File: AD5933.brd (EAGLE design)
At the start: 82.8 x 53.3 mm, 80 parts, among them U1 ADG1604BRUZ, U10 ADP3303ARZ-3.3, U11 AD5242BRZ1M, U12 AD5245BRJZ100-R2, U2 AD5933YRSZ, U3 AD5242BRZ1M, U4 AD8606ARZ, U5 ADG1604BRUZ, U7 AD8606ARZ, U8 LTC6904MPMS8TRPBF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

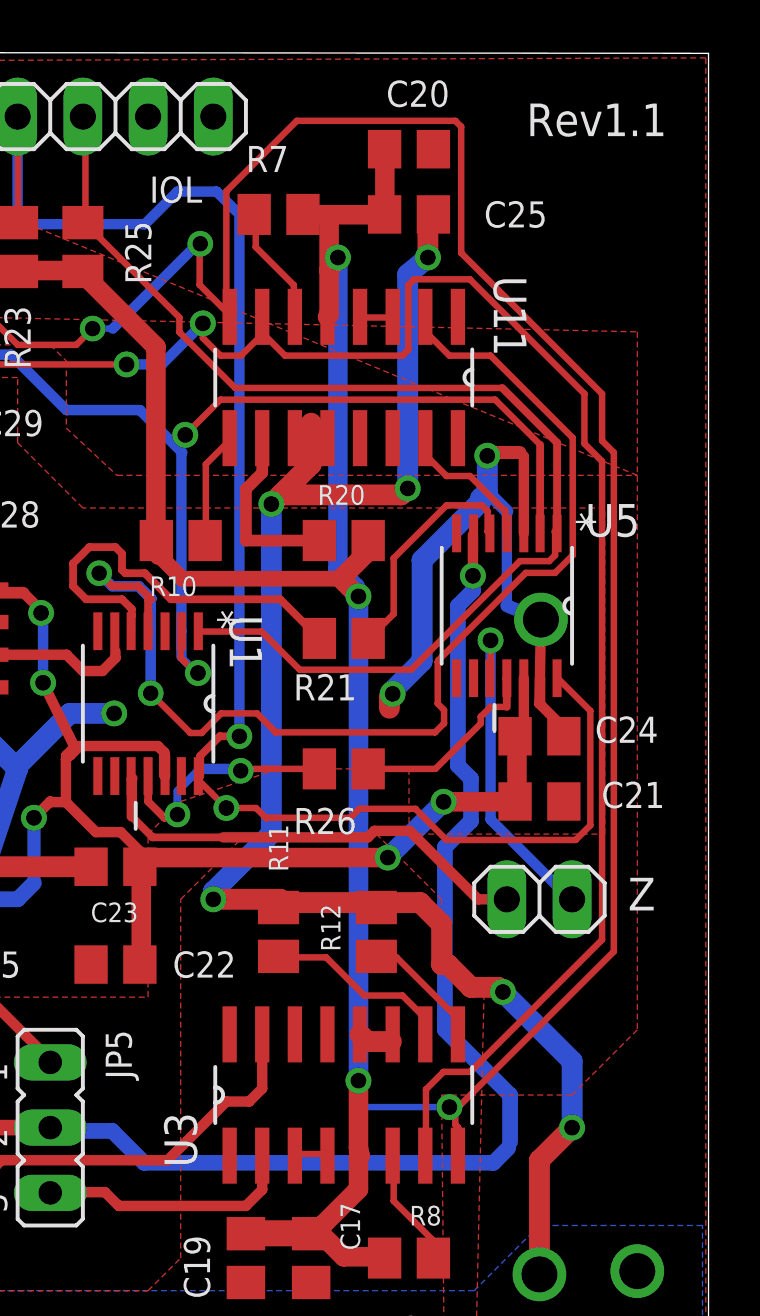
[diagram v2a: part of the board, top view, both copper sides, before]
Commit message: Fixed ad5242 open ckt bug, rev 1.2
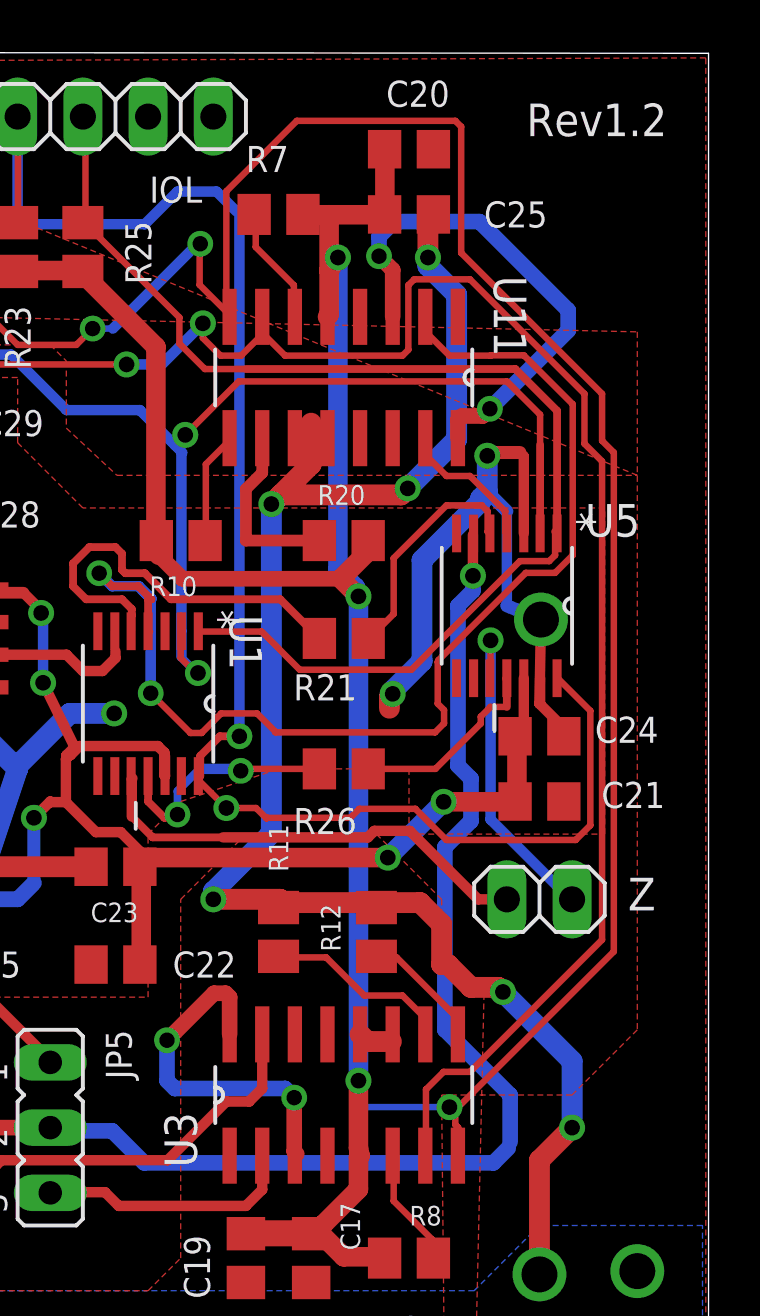
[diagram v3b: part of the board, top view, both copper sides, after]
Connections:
- net U11_W1: now also U11.16; no longer U11.4
- net U3_W1: now also U3.16; no longer U3.4
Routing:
- net U11_W1: track 1.28 -> 19.7 mm, vias 0 -> 2
- net U3_W1: track 1.32 -> 13.8 mm, vias 0 -> 2
- net EN1: track 57.2 -> 58.5 mm
- net A01: track 47.4 -> 48.4 mm
- net GND: track 193.5 -> 194.4 mm
- net U1_S1: track 45.5 -> 46.3 mm
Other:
- board text added: "Rev1.2"
- board text removed: "Rev1.1"
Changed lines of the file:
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@@
 <wire x1="82.784" y1="53.263403125" x2="0.031021875" y2="53.3354375" width="0" layer="20"/>
 <wire x1="0.031021875" y1="53.3354375" x2="0" y2="0" width="0" layer="20"/>
-<text x="75.692" y="50.038" size="1.27" layer="25">Rev1.1</text>
+<text x="75.692" y="50.038" size="1.27" layer="25">Rev1.2</text>
 <text x="66.167" y="3.048" size="1.016" layer="25">IDEA Lab, UTD</text>
 <text x="65.024" y="1.524" size="1.016" layer="25">Athul Asokan Thulasi</text>
@@
 <wire x1="62.2935" y1="30.7467" x2="62.2554" y2="30.7594" width="0.254" layer="1"/>
 <wire x1="53.3781" y1="50.7492" x2="53.34" y2="50.8" width="0.254" layer="16"/>
-<wire x1="63.7794" y1="39.7764" x2="74.4728" y2="39.7764" width="0.254" layer="1"/>
-<wire x1="62.4078" y1="38.4048" x2="63.7794" y2="39.7764" width="0.254" layer="1"/>
+<wire x1="62.4078" y1="38.4048" x2="64.4906" y2="40.4876" width="0.254" layer="1"/>
 <wire x1="62.00775" y1="38.00475" x2="62.4078" y2="38.4048" width="0.4064" layer="16"/>
 <wire x1="53.3781" y1="50.7492" x2="53.3781" y2="46.7487" width="0.254" layer="1"/>
@@
 <wire x1="62.8142" y1="29.1338" x2="62.9031" y2="29.1338" width="0.6096" layer="16"/>
 <wire x1="76.2254" y1="34.5694" x2="76.2254" y2="38.0238" width="0.3048" layer="1"/>
-<wire x1="76.2254" y1="38.0238" x2="74.4728" y2="39.7764" width="0.254" layer="1"/>
 <wire x1="62.9031" y1="29.1338" x2="62.8142" y2="29.1338" width="0.254" layer="1"/>
 <wire x1="62.8142" y1="29.1338" x2="62.23" y2="29.718" width="0.254" layer="1"/>
@@
 <wire x1="53.467" y1="41.529" x2="55.626" y2="41.529" width="0.4064" layer="16"/>
 <wire x1="55.626" y1="41.529" x2="57.785" y2="39.37" width="0.4064" layer="16"/>
+<wire x1="64.4906" y1="40.4876" x2="74.93" y2="40.4876" width="0.254" layer="1"/>
+<wire x1="74.93" y1="40.4876" x2="76.2254" y2="39.1922" width="0.254" layer="1"/>
+<wire x1="76.2254" y1="39.1922" x2="76.2254" y2="38.0238" width="0.254" layer="1"/>
 </signal>
 <signal name="A01">
@@
 <wire x1="76.8096" y1="34.5186" x2="76.8858" y2="34.5694" width="0.254" layer="1"/>
 <wire x1="62.1792" y1="42.9768" x2="58.5216" y2="46.6344" width="0.254" layer="1"/>
-<wire x1="62.1792" y1="42.4053" x2="62.1792" y2="42.9768" width="0.254" layer="1"/>
-<wire x1="64.3509" y1="40.2336" x2="62.1792" y2="42.4053" width="0.254" layer="1"/>
-<wire x1="73.6092" y1="40.2336" x2="64.3509" y2="40.2336" width="0.254" layer="1"/>
+<wire x1="62.1792" y1="41.9608" x2="62.1792" y2="42.9768" width="0.254" layer="1"/>
 <wire x1="58.5216" y1="46.6344" x2="58.42" y2="46.67" width="0.254" layer="1"/>
 <wire x1="76.8096" y1="34.6329" x2="76.8858" y2="34.5694" width="0.254" layer="1"/>
 <wire x1="76.8096" y1="34.6329" x2="76.8858" y2="34.7091" width="0.3048" layer="1"/>
-<wire x1="76.8858" y1="34.7091" x2="76.8858" y2="38.1" width="0.3048" layer="1"/>
-<wire x1="76.8858" y1="38.1" x2="74.7522" y2="40.2336" width="0.3048" layer="1"/>
-<wire x1="74.7522" y1="40.2336" x2="73.6092" y2="40.2336" width="0.254" layer="1"/>
+<wire x1="76.8858" y1="34.7091" x2="76.8858" y2="39.3446" width="0.3048" layer="1"/>
+<wire x1="75.2602" y1="40.9702" x2="64.77" y2="40.9702" width="0.3048" layer="1"/>
+<wire x1="62.1792" y1="41.9608" x2="63.1698" y2="40.9702" width="0.254" layer="1"/>
+<wire x1="63.1698" y1="40.9702" x2="64.77" y2="40.9702" width="0.254" layer="1"/>
+<wire x1="75.2602" y1="40.9702" x2="76.8858" y2="39.3446" width="0.3048" layer="1"/>
 </signal>
 <signal name="A11">
@@
 <via x="71.8566" y="45.3136" extent="1-16" drill="0.6096"/>
 <wire x1="71.8566" y1="45.3136" x2="71.882" y2="45.466" width="0.8128" layer="16"/>
-<wire x1="71.8566" y1="45.3136" x2="71.0692" y2="44.6532" width="0.8128" layer="16"/>
-<wire x1="71.0692" y1="44.6532" x2="71.0692" y2="36.322" width="0.8128" layer="16"/>
 <via x="71.0692" y="36.322" extent="1-16" drill="0.6096"/>
 <wire x1="71.0692" y1="36.322" x2="70.8152" y2="36.068" width="0.8128" layer="1"/>
@@
 <wire x1="26.67" y1="30.48" x2="29.21" y2="30.48" width="0.8128" layer="16"/>
 <wire x1="29.21" y1="30.48" x2="29.21" y2="26.416" width="0.8128" layer="16"/>
+<wire x1="71.0692" y1="36.322" x2="72.9742" y2="38.227" width="0.8128" layer="16"/>
+<wire x1="72.9742" y1="38.227" x2="72.9742" y2="43.8658" width="0.8128" layer="16"/>
+<wire x1="72.9742" y1="43.8658" x2="71.8566" y2="44.9834" width="0.8128" layer="16"/>
+<wire x1="71.8566" y1="44.9834" x2="71.8566" y2="45.3136" width="0.8128" layer="16"/>
 </signal>
 <signal name="N$7">
@@
 <signal name="U3_W1">
 <contactref element="U3" pad="3"/>
-<contactref element="U3" pad="4"/>
-<wire x1="67.8942" y1="10.4013" x2="66.7512" y2="10.4013" width="0.254" layer="1"/>
 <wire x1="66.7512" y1="10.4013" x2="66.675" y2="10.3378" width="0.254" layer="1"/>
-<wire x1="67.8942" y1="10.4013" x2="67.945" y2="10.3378" width="0.254" layer="1"/>
+<contactref element="U3" pad="16"/>
+<wire x1="66.7512" y1="10.4013" x2="66.6496" y2="10.5029" width="0.6096" layer="1"/>
+<wire x1="66.6496" y1="10.5029" x2="66.6496" y2="12.5984" width="0.6096" layer="1"/>
+<via x="66.6496" y="12.5984" extent="1-16" drill="0.6" shape="square"/>
+<wire x1="66.6496" y1="12.5984" x2="66.294" y2="12.954" width="0.6096" layer="16"/>
+<wire x1="66.294" y1="12.954" x2="62.0014" y2="12.954" width="0.6096" layer="16"/>
+<wire x1="62.0014" y1="12.954" x2="61.6966" y2="13.2588" width="0.6096" layer="16"/>
+<wire x1="61.6966" y1="13.2588" x2="61.6966" y2="14.8336" width="0.6096" layer="16"/>
+<via x="61.6966" y="14.8336" extent="1-16" drill="0.6" shape="square"/>
+<wire x1="61.6966" y1="14.8336" x2="63.5254" y2="16.6624" width="0.6096" layer="1"/>
+<wire x1="63.5254" y1="16.6624" x2="63.9826" y2="16.6624" width="0.6096" layer="1"/>
+<wire x1="63.9826" y1="16.6624" x2="64.135" y2="16.51" width="0.6096" layer="1"/>
+<wire x1="64.135" y1="16.51" x2="64.135" y2="15.0622" width="0.6096" layer="1"/>
 </signal>
 <signal name="U11_W2">
@@
 <signal name="U11_W1">
 <contactref element="U11" pad="3"/>
-<contactref element="U11" pad="4"/>
-<wire x1="70.4088" y1="42.9768" x2="69.2658" y2="42.9768" width="0.254" layer="1"/>
-<wire x1="69.2658" y1="42.9768" x2="69.215" y2="43.0022" width="0.254" layer="1"/>
 <wire x1="70.4088" y1="42.9768" x2="70.485" y2="43.0022" width="0.254" layer="1"/>
+<contactref element="U11" pad="16"/>
+<wire x1="73.025" y1="38.2778" x2="73.025" y2="38.989" width="0.6096" layer="1"/>
+<wire x1="73.025" y1="38.989" x2="73.1774" y2="39.1414" width="0.6096" layer="1"/>
+<wire x1="73.1774" y1="39.1414" x2="73.9902" y2="39.1414" width="0.6096" layer="1"/>
+<wire x1="73.9902" y1="39.1414" x2="74.2696" y2="39.4208" width="0.6096" layer="1"/>
+<via x="74.2696" y="39.4208" extent="1-16" drill="0.6" shape="square"/>
+<wire x1="74.2696" y1="39.4208" x2="77.3176" y2="42.4688" width="0.6096" layer="16"/>
+<wire x1="77.3176" y1="42.4688" x2="77.3176" y2="43.2562" width="0.6096" layer="16"/>
+<wire x1="77.3176" y1="43.2562" x2="73.8632" y2="46.7106" width="0.6096" layer="16"/>
+<wire x1="73.8632" y1="46.7106" x2="70.5358" y2="46.7106" width="0.6096" layer="16"/>
+<wire x1="70.5358" y1="46.7106" x2="69.9516" y2="46.1264" width="0.6096" layer="16"/>
+<wire x1="69.9516" y1="46.1264" x2="69.9516" y2="45.3644" width="0.6096" layer="16"/>
+<via x="69.9516" y="45.3644" extent="1-16" drill="0.6" shape="square"/>
+<wire x1="69.9516" y1="45.3644" x2="70.485" y2="44.831" width="0.6096" layer="1"/>
+<wire x1="70.485" y1="44.831" x2="70.485" y2="43.0022" width="0.6096" layer="1"/>
 </signal>
 <signal name="N$10">
@@
 <wire x1="76.8096" y1="33.0327" x2="75.6666" y2="33.0327" width="0.254" layer="1"/>
 <wire x1="77.4954" y1="33.7185" x2="76.8096" y2="33.0327" width="0.254" layer="1"/>
-<wire x1="77.4954" y1="38.2905" x2="77.4954" y2="33.7185" width="0.254" layer="1"/>
-<wire x1="74.295" y1="41.4909" x2="77.4954" y2="38.2905" width="0.254" layer="1"/>
+<wire x1="77.4954" y1="39.5986" x2="77.4954" y2="33.7185" width="0.254" layer="1"/>
 <wire x1="72.6948" y1="41.4909" x2="74.295" y2="41.4909" width="0.254" layer="1"/>
 <wire x1="71.7804" y1="42.4053" x2="72.6948" y2="41.4909" width="0.254" layer="1"/>
@@
 <wire x1="60.6044" y1="32.512" x2="61.087" y2="32.0294" width="0.4064" layer="16"/>
 <wire x1="61.087" y1="32.0294" x2="61.087" y2="32.004" width="0.4064" layer="16"/>
+<wire x1="74.295" y1="41.4909" x2="74.3077" y2="41.5036" width="0.254" layer="1"/>
+<wire x1="74.3077" y1="41.5036" x2="75.5904" y2="41.5036" width="0.254" layer="1"/>
+<wire x1="75.5904" y1="41.5036" x2="77.4954" y2="39.5986" width="0.254" layer="1"/>
 </signal>
 <signal name="U7_INA-">

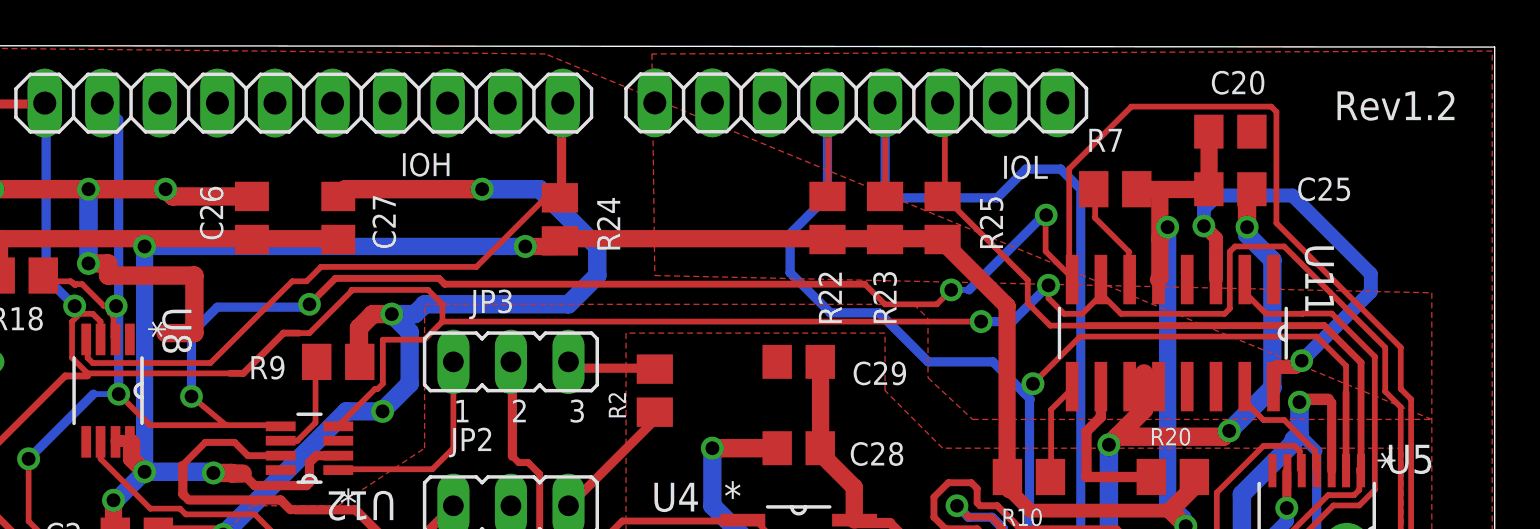
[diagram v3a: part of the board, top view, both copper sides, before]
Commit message: fix ad5245 address to 0x2d to remove iic bus conflict with ad5242-u3
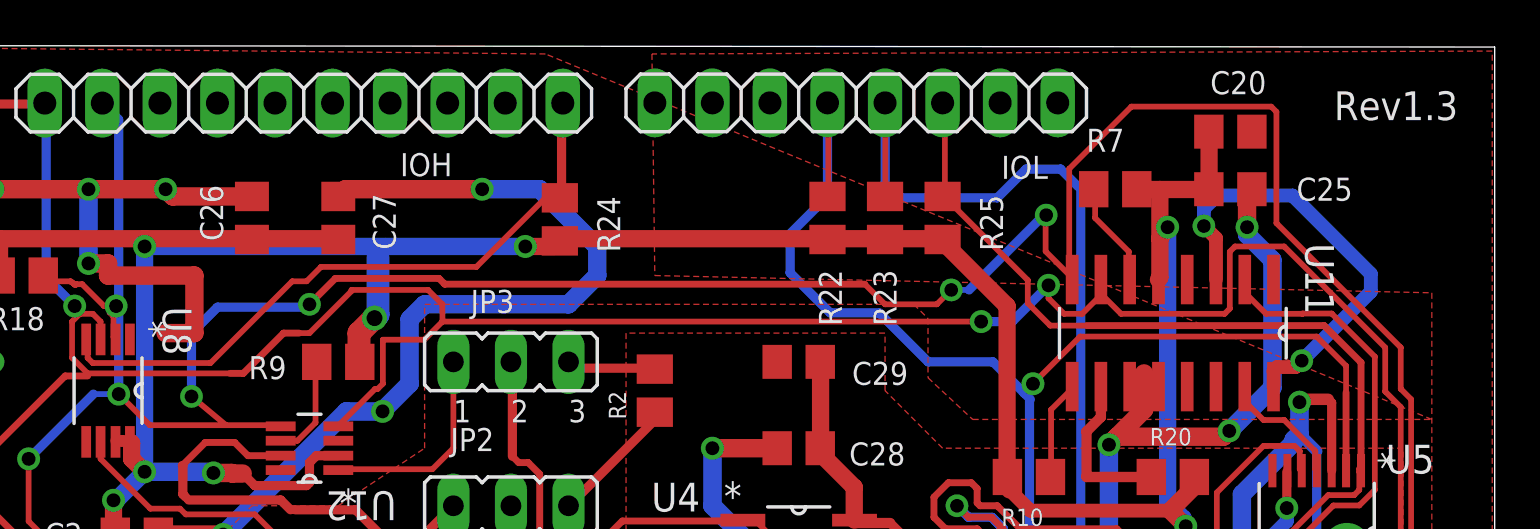
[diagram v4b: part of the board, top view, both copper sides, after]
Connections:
- net GND: no longer R9.1
- net VDD: now also R9.1
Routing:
- net VDD: track 187.8 -> 193.5 mm, vias 8 -> 9
- net GND: track 194.4 -> 189.9 mm, vias 22 -> 21
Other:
- board text added: "Rev1.3"
- board text removed: "Rev1.2"
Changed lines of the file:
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@@
 <wire x1="82.784" y1="53.263403125" x2="0.031021875" y2="53.3354375" width="0" layer="20"/>
 <wire x1="0.031021875" y1="53.3354375" x2="0" y2="0" width="0" layer="20"/>
-<text x="75.692" y="50.038" size="1.27" layer="25">Rev1.2</text>
+<text x="75.692" y="50.038" size="1.27" layer="25">Rev1.3</text>
 <text x="66.167" y="3.048" size="1.016" layer="25">IDEA Lab, UTD</text>
 <text x="65.024" y="1.524" size="1.016" layer="25">Athul Asokan Thulasi</text>
@@
 <wire x1="68.3514" y1="45.3136" x2="68.0085" y2="44.8056" width="0.762" layer="1"/>
 <wire x1="69.0372" y1="32.4612" x2="69.1515" y2="32.1183" width="0.762" layer="16"/>
-<wire x1="40.005" y1="44.4627" x2="23.2029" y2="44.4627" width="0.762" layer="16"/>
+<wire x1="40.005" y1="44.4627" x2="33.8328" y2="44.4627" width="0.762" layer="16"/>
+<wire x1="33.8328" y1="44.4627" x2="23.2029" y2="44.4627" width="0.762" layer="16"/>
 <wire x1="41.2623" y1="44.4627" x2="40.005" y2="44.4627" width="0.762" layer="1"/>
 <wire x1="41.2623" y1="44.4627" x2="41.528928125" y2="44.7089625" width="0.762" layer="1"/>
@@
 <wire x1="21.9456" y1="35.8394" x2="21.9456" y2="35.8902" width="0.4064" layer="1"/>
 <wire x1="21.9202" y1="35.8394" x2="21.9456" y2="35.8394" width="0.4064" layer="1"/>
+<contactref element="R9" pad="1"/>
+<wire x1="32.7" y1="39.37" x2="32.6644" y2="39.4056" width="1.016" layer="1"/>
+<wire x1="32.6644" y1="39.4056" x2="32.6644" y2="40.64" width="1.016" layer="1"/>
+<wire x1="32.6644" y1="40.64" x2="33.3248" y2="41.3004" width="1.016" layer="1"/>
+<wire x1="33.3248" y1="41.3004" x2="33.3502" y2="41.3004" width="1.016" layer="1"/>
+<via x="33.3502" y="41.3004" extent="1-16" drill="0.7"/>
+<wire x1="33.3502" y1="41.3004" x2="33.5026" y2="41.4528" width="1.016" layer="16"/>
+<wire x1="33.5026" y1="41.4528" x2="33.5026" y2="43.942" width="1.016" layer="16"/>
+<wire x1="33.5026" y1="43.942" x2="33.8328" y2="44.2722" width="0.4064" layer="16"/>
+<wire x1="33.8328" y1="44.2722" x2="33.8328" y2="44.4627" width="0.4064" layer="16"/>
 </signal>
 <signal name="U1_S3">
@@
 <contactref element="U11" pad="11"/>
 <contactref element="U12" pad="3"/>
-<contactref element="R9" pad="1"/>
 <contactref element="POWER" pad="7"/>
 <contactref element="POWER" pad="6"/>
@@
 <wire x1="8.89" y1="36.83" x2="8.1534" y2="36.0934" width="0.8128" layer="16"/>
 <wire x1="8.1534" y1="36.0934" x2="8.1534" y2="33.7566" width="0.8128" layer="16"/>
-<wire x1="32.7" y1="39.37" x2="32.6644" y2="39.4056" width="0.8128" layer="1"/>
-<wire x1="32.6644" y1="39.4056" x2="32.6644" y2="40.8686" width="0.8128" layer="1"/>
-<wire x1="32.6644" y1="40.8686" x2="33.274" y2="41.4782" width="0.8128" layer="1"/>
-<wire x1="33.274" y1="41.4782" x2="34.1122" y2="41.4782" width="0.8128" layer="1"/>
-<via x="34.1122" y="41.4782" extent="1-16" drill="0.6096"/>
-<wire x1="34.1122" y1="41.4782" x2="34.8996" y2="40.6908" width="0.8128" layer="16"/>
-<wire x1="34.8996" y1="40.6908" x2="34.8996" y2="38.4048" width="0.8128" layer="16"/>
+<wire x1="34.8996" y1="41.2496" x2="34.8996" y2="38.4048" width="0.8128" layer="16"/>
 <wire x1="34.8996" y1="38.4048" x2="33.7058" y2="37.211" width="0.8128" layer="16"/>
 <wire x1="33.7058" y1="37.211" x2="33.7058" y2="37.1856" width="0.8128" layer="16"/>
@@
 <wire x1="43.18" y1="43.18" x2="41.91" y2="41.91" width="0.8128" layer="16"/>
 <wire x1="41.91" y1="41.91" x2="35.56" y2="41.91" width="0.8128" layer="16"/>
-<wire x1="35.56" y1="41.91" x2="35.1282" y2="41.4782" width="0.8128" layer="16"/>
-<wire x1="35.1282" y1="41.4782" x2="34.1122" y2="41.4782" width="0.8128" layer="16"/>
+<wire x1="35.56" y1="41.91" x2="34.8996" y2="41.2496" width="0.8128" layer="16"/>
 <wire x1="23.81" y1="31.75" x2="26.67" y2="31.75" width="0.8128" layer="1"/>
 <via x="26.67" y="31.75" extent="1-16" drill="0.6096"/>
